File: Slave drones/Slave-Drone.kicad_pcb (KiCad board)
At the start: 4 copper layers, 32 x 32 mm, 45 parts, among them J1 Conn_01x02, J2 Conn_01x02, J3 Conn_01x02, J4 Conn_01x02, J5 USB_C_Receptacle_USB2.0_16P, J6 Conn_01x02, SW1 SW_Push, SW2 SW_Push, U1 MPU6500, U2 QMC5883L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

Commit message: silkscreen art
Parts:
- added G***: LOGO, LOGO, B.Cu at (121.4, 79.7)

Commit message: BOM
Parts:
- U1, U2: moved to F.Cu
- moved U1 20.1 mm to (128.1, 78.9)
- moved U2 16.1 mm to (125.0, 82.3), turned to 0 degrees
- moved C2 0.60 mm to (103.5, 82.4)
- moved MOSFET1 0.21 mm to (124.4, 78.5)
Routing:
- net GND: track 24.2 -> 42.5 mm, vias 21 -> 20
- net /SDA: track 17.9 -> 33.9 mm, vias 3 -> 5
- net /SCL: track 16.3 -> 32.0 mm, vias 3 -> 4
- net (no net): track 2.89 -> 0.00 mm, vias 2 -> 0
- net +3.3V: track 24.1 -> 25.4 mm, vias 6 -> 8
- net /Motor_Power: track 73.6 -> 72.5 mm, vias 2 -> 4

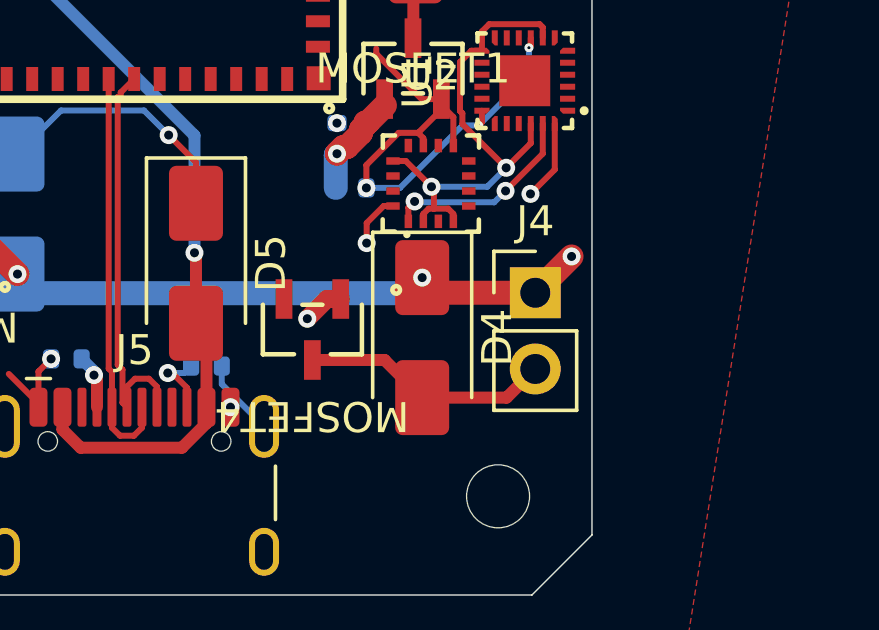
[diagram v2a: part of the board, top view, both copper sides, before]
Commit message: changed QMC5338L to QMC5338P
Has the same symbol/footprint but slightly different wiring
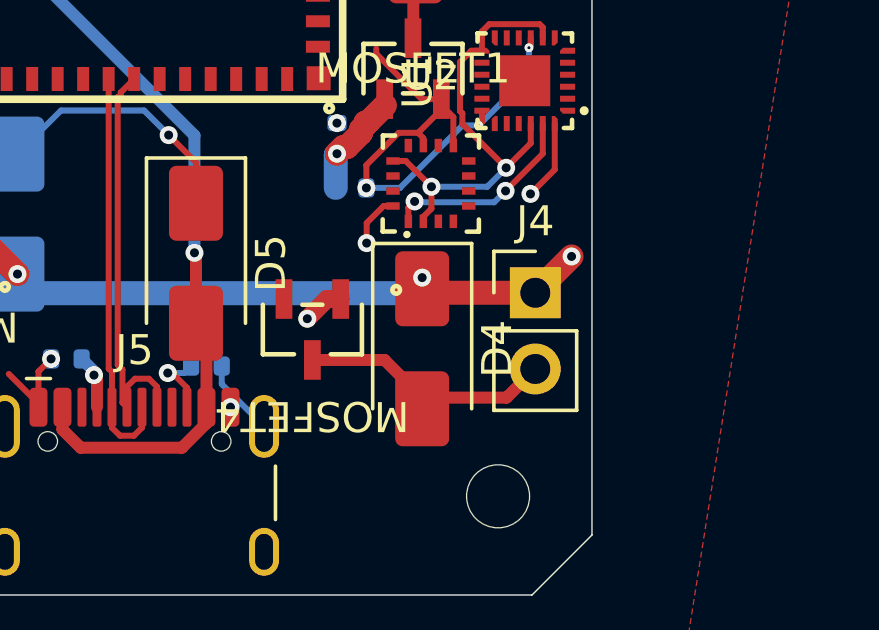
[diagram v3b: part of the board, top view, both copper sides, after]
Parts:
- moved D4 0.37 mm to (124.7, 87.8)
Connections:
- U2 pad 4: +3.3V -> unconnected-(U2-S1-Pad4)
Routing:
- net +3.3V: track 25.4 -> 24.4 mm
